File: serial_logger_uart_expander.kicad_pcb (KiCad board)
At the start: 2 copper layers, 95 x 65 mm, 55 parts, among them J1 CN6, J2 CN8, J3 CN5, J4 CN9, J5 Screw_Terminal_01x10, J6 Screw_Terminal_01x10, U1 M74HC4851, U10 2N7002PS, U11 2N7002PS, U12 2N7002PS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

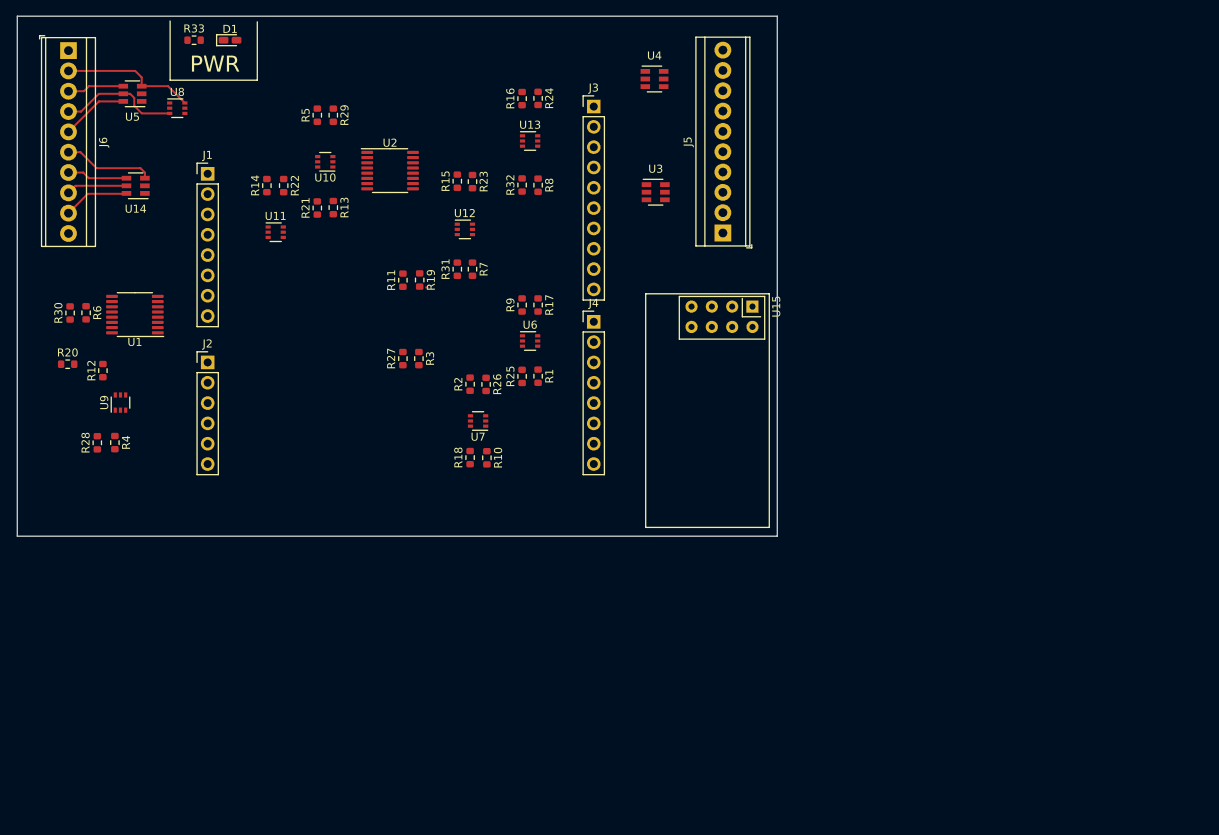
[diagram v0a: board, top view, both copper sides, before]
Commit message: rearranged components and traces
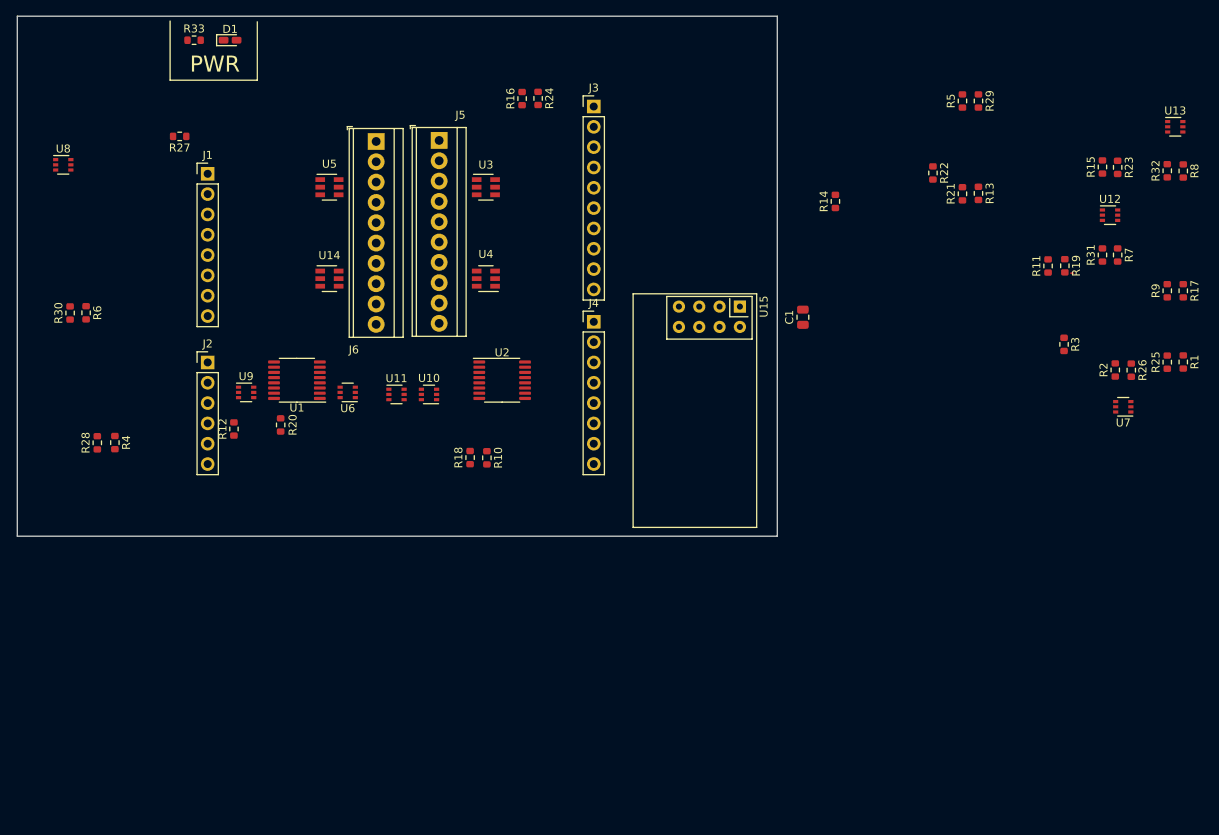
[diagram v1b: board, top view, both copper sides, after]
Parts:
- added C1: 10u, Capacitor_SMD:C_0805_2012Metric, F.Cu at (203.2, 87.6)
- moved R22 81.2 mm to (219.5, 69.6)
- moved R1 80.7 mm to (250.7, 93.2)
- moved R11 80.7 mm to (233.8, 81.2)
- moved R13 80.7 mm to (225.1, 72.1)
- moved R15 80.7 mm to (240.6, 68.8)
- moved R17 80.7 mm to (250.7, 84.3)
- moved R2 80.7 mm to (242.2, 94.2)
- moved R21 80.7 mm to (223.1, 72.2)
- moved R25 80.7 mm to (248.7, 93.2)
- moved R26 80.7 mm to (244.2, 94.2)
- moved R29 80.7 mm to (225.1, 60.6)
- moved R3 80.7 mm to (235.8, 91.0)
- moved R31 80.7 mm to (240.6, 79.8)
- moved R32 80.7 mm to (248.7, 69.3)
- moved R5 80.7 mm to (223.1, 60.6)
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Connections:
- U14 pad 1: Net-(U14-Pad1) -> RX1
- U14 pad 3: TX1 -> Net-(U14-Pad3)
- U14 pad 4: RX1 -> RX0
- U14 pad 6: RX0 -> Net-(U14-Pad6)
- U3 pad 1: Net-(U3-Pad1) -> TX7
- U3 pad 3: TX7 -> TX5
- U3 pad 4: RX7 -> RX6
- U3 pad 6: RX6 -> RX7
- U4 pad 1: Net-(U4-Pad1) -> RX5
- U4 pad 3: TX5 -> Net-(U4-Pad3)
- U4 pad 4: RX5 -> Net-(U4-Pad4)
- U4 pad 5: TX4 -> RX4
- U4 pad 6: RX4 -> TX4
- U5 pad 1: Net-(U5-Pad1) -> TX3
- U5 pad 3: TX3 -> TX1
- U5 pad 4: RX3 -> RX2
- U5 pad 6: RX2 -> RX3
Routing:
- net TX3: track 16.9 -> 0.00 mm
- net TX2: track 15.2 -> 0.00 mm
- net TX1: track 11.3 -> 0.00 mm
- net RX2: track 8.43 -> 0.00 mm
- net RX0: track 8.27 -> 0.00 mm
- net TX0: track 7.61 -> 0.00 mm
- net RX1: track 7.54 -> 0.00 mm
- net RX3: track 7.11 -> 0.00 mm
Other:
- net class JLCPCB added: clearance 0.127, trace_width 0.127, via_dia 0.8, via_drill 0.4
- rule trace_min: 0.2 -> 0.127
- rule via_min_drill: 0.3 -> 0.2

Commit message: completed design, no gerbers or BOM.
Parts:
- moved R23 127.6 mm to (127.0, 123.0)
- moved R8 126.0 mm to (138.3, 126.2), turned to 180 degrees
- moved U13 125.9 mm to (138.2, 122.1)
- moved R32 123.5 mm to (138.3, 124.5), turned to 180 degrees
- moved R11 123.3 mm to (117.2, 121.1), turned to 270 degrees
- moved U12 121.6 mm to (129.6, 122.2), turned to 180 degrees
- moved R15 121.2 mm to (132.2, 123.0)
- moved R3 120.7 mm to (119.9, 124.5), turned to 180 degrees
- moved R19 120.3 mm to (122.5, 121.2), turned to 90 degrees
- moved R7 119.8 mm to (129.6, 119.8), turned to 0 degrees
- moved R31 117.4 mm to (129.6, 118.0), turned to 0 degrees
- moved R17 95.4 mm to (163.6, 123.1)
- moved R29 93.5 mm to (157.0, 124.6), turned to 180 degrees
- moved R5 93.2 mm to (157.1, 126.3), turned to 180 degrees
- moved R9 88.8 mm to (168.9, 123.1)
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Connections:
- U14 pad 1: RX1 -> Net-(U14-Pad1)
- U14 pad 3: Net-(U14-Pad3) -> TX1
- U14 pad 4: RX0 -> RX1
- U14 pad 6: Net-(U14-Pad6) -> RX0
- U3 pad 1: TX7 -> Net-(U3-Pad1)
- U3 pad 3: TX5 -> TX7
- U3 pad 4: RX6 -> RX7
- U3 pad 6: RX7 -> RX6
- U4 pad 1: RX5 -> Net-(U4-Pad1)
- U4 pad 3: Net-(U4-Pad3) -> TX5
- U4 pad 4: Net-(U4-Pad4) -> RX5
- U4 pad 5: RX4 -> TX4
- U4 pad 6: TX4 -> RX4
- U5 pad 1: TX3 -> Net-(U5-Pad1)
- U5 pad 3: TX1 -> TX3
- U5 pad 4: RX2 -> RX3
- U5 pad 6: RX3 -> RX2
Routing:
- net RX_CH1: track 0.00 -> 83.9 mm, vias 0 -> 2
- net RX_CH2: track 0.00 -> 79.2 mm, vias 0 -> 2
- net TX_CH5: track 0.00 -> 57.6 mm, vias 0 -> 2
- net RX_CH3: track 0.00 -> 55.9 mm, vias 0 -> 2
- net TX_CH4: track 0.00 -> 54.2 mm
- net +3V3: track 0.00 -> 52.4 mm
- net RX_CH0: track 0.00 -> 47.9 mm, vias 0 -> 2
- net TX_CH7: track 0.00 -> 45.8 mm, vias 0 -> 2
- net RX_CH6: track 0.00 -> 41.3 mm, vias 0 -> 4
- net TX_CH1: track 0.00 -> 41.2 mm, vias 0 -> 2
- net DATA_TX: track 0.00 -> 41.0 mm, vias 0 -> 1
- net RX_CH4: track 0.00 -> 40.8 mm, vias 0 -> 2
- net TX_CH3: track 0.00 -> 38.8 mm, vias 0 -> 2
- net TX_CH2: track 0.00 -> 38.7 mm, vias 0 -> 2
- net RX_INH: track 0.00 -> 38.6 mm, vias 0 -> 1
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- added copper zone on F.Cu, net +3V3
- added copper zone on B.Cu, net GND
- added copper zone on F.Cu, net VBUS
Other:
- board size 95 x 65 mm -> 95 x 100 mm

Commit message: v0.0 completed
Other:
- outline, holes or cut-outs redrawn
- board text added: "3V3"
- board text added: "5V"
- board text added: "8:1 UART MUX v0.0"
- board text added: "CE"
- board text added: "DATA_RX"
- board text added: "DATA_TX"
- board text added: "GND"
- board text added: "IRQ"
- board text added: "J. Gillispie 2021"
- board text added: "LD2"
- board text added: "MISO"
- board text added: "MOSI"
- board text added: "RX0"
- board text added: "RX1"
- board text added: "RX2"
- board text added: "RX3"
- board text added: "RX4"
- board text added: "RX5"
- board text added: "RX6"
- board text added: "RX7"
- board text added: "RX_A"
- board text added: "RX_B"
- board text added: "RX_C"
- board text added: "RX_INH"
- board text added: "SCK"
- board text added: "TX0"
- board text added: "TX1"
- board text added: "TX2"
- board text added: "TX3"
- board text added: "TX4"
- board text added: "TX5"
- board text added: "TX6"
- board text added: "TX7"
- board text added: "TX_A"
- board text added: "TX_B"
- board text added: "TX_C"
- board text added: "TX_INH"
- board text added: "VBUS"
- board text added: "VCOM_RX"
- board text added: "VCOM_TX"
- board text added: "~CS"
- board text added: "~RST"

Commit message: completed v0.1 design with 2n7002; no BOM or gerbers
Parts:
- removed the J5 at (156.8, 138.9)
- removed the R21 at (159.6, 121.4)
- removed U10, U11, U12, U13, U8, U9: 2N7002PS, my_lib:2N7002PS_NEXPERA_SOT-363
- removed U14: ESDA17-5SC6, my_lib:ESDA17-5SC6_SOT23-6L
- removed the U3 at (162.7, 132.6)
- added J1: Screw_Terminal_01x10, TerminalBlock_TE-Connectivity:TerminalBlock_TE_1-282834-0_1x10_P2.54mm_Horizontal, F.Cu at (126.4, 138.8)
- added Q1: 2N7002, Package_TO_SOT_SMD:SOT-23, F.Cu at (124.1, 124.5)
- added Q10: 2N7002, Package_TO_SOT_SMD:SOT-23, F.Cu at (143.0, 124.5)
- added Q11: 2N7002, Package_TO_SOT_SMD:SOT-23, F.Cu at (155.1, 124.5)
- added Q12: 2N7002, Package_TO_SOT_SMD:SOT-23, F.Cu at (171.2, 124.5)
- added Q13: 2N7002, Package_TO_SOT_SMD:SOT-23, F.Cu at (178.4, 125.7)
- added Q14: 2N7002, Package_TO_SOT_SMD:SOT-23, F.Cu at (135.4, 125.8)
- added Q15: 2N7002, Package_TO_SOT_SMD:SOT-23, F.Cu at (150.6, 125.7)
- added Q16: 2N7002, Package_TO_SOT_SMD:SOT-23, F.Cu at (162.3, 125.7)
- added Q2: 2N7002, Package_TO_SOT_SMD:SOT-23, F.Cu at (139.3, 124.5)
- added Q3: 2N7002, Package_TO_SOT_SMD:SOT-23, F.Cu at (158.7, 124.5)
- added Q4: 2N7002, Package_TO_SOT_SMD:SOT-23, F.Cu at (174.8, 124.5)
- added Q5: 2N7002, Package_TO_SOT_SMD:SOT-23, F.Cu at (131.2, 125.8)
- added Q6: 2N7002, Package_TO_SOT_SMD:SOT-23, F.Cu at (146.6, 125.7)
- added Q7: 2N7002, Package_TO_SOT_SMD:SOT-23, F.Cu at (166.5, 125.7)
- added Q8: 2N7002, Package_TO_SOT_SMD:SOT-23, F.Cu at (182.6, 125.7)
- added Q9: 2N7002, Package_TO_SOT_SMD:SOT-23, F.Cu at (127.7, 124.5)
- added R11: 10k, Resistor_SMD:R_0603_1608Metric, F.Cu at (141.1, 132.0)
- U6, U7: value 2N7002PS -> ESDA17-5SC6; footprint my_lib:2N7002PS_NEXPERA_SOT-363 -> my_lib:ESDA17-5SC6_SOT23-6L
- moved R10 53.6 mm to (134.4, 132.1), turned to 180 degrees
- moved R2 52.3 mm to (132.3, 118.2), turned to 90 degrees
- moved R26 51.2 mm to (134.4, 129.8), turned to 180 degrees
- moved R8 46.0 mm to (183.6, 118.2), turned to 90 degrees
- moved R18 45.9 mm to (136.4, 118.2), turned to 90 degrees
- moved U4 45.3 mm to (130.8, 130.9)
- moved R7 44.3 mm to (173.9, 118.2), turned to 90 degrees
- moved R23 43.5 mm to (170.3, 118.2), turned to 90 degrees
- moved R16 43.2 mm to (177.4, 132.1), turned to 180 degrees
- moved R1 43.2 mm to (123.1, 118.2), turned to 90 degrees
- moved R9 42.6 mm to (127.3, 132.1), turned to 0 degrees
- moved R31 42.1 mm to (170.1, 129.7)
- moved R25 40.3 mm to (127.3, 129.8)
- moved R32 39.5 mm to (177.4, 129.7)
- moved R15 38.9 mm to (170.1, 132.0), turned to 0 degrees
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- renumbered J1 to J2, J2 to J3, J3 to J4, J4 to J5, R11 to R21, U15 to U3
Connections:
- R1 pad 1: TX_CH6 -> RX_CH7
- R10 pad 1: TX_CH5 -> VBUS
- R10 pad 2: +3V3 -> RX6
- R12 pad 1: TX_CH1 -> VBUS
- R12 pad 2: +3V3 -> RX4
- R13 pad 1: RX_CH7 -> VBUS
- R13 pad 2: +3V3 -> RX3
- R14 pad 1: RX_CH5 -> VBUS
- R14 pad 2: +3V3 -> RX2
- R15 pad 1: RX_CH3 -> VBUS
- R15 pad 2: +3V3 -> RX1
- R16 pad 1: RX_CH1 -> VBUS
- R16 pad 2: +3V3 -> RX0
- R17 pad 1: VBUS -> TX_CH7
- R17 pad 2: TX7 -> +3V3
- R18 pad 1: VBUS -> TX_CH6
- R18 pad 2: TX5 -> +3V3
- R19 pad 1: VBUS -> TX_CH5
- R19 pad 2: TX3 -> +3V3
- R2 pad 1: TX_CH4 -> RX_CH6
- R20 pad 1: VBUS -> TX_CH4
- R20 pad 2: TX1 -> +3V3
- R22 pad 1: VBUS -> TX_CH2
- R22 pad 2: RX5 -> +3V3
- R23 pad 1: VBUS -> TX_CH1
- R23 pad 2: RX3 -> +3V3
- R24 pad 1: VBUS -> TX_CH0
- R24 pad 2: RX1 -> +3V3
- R25 pad 2: TX6 -> TX7
- R26 pad 2: TX4 -> TX6
- R27 pad 2: TX2 -> TX5
- R28 pad 2: TX0 -> TX4
- R29 pad 2: RX6 -> TX3
- R3 pad 1: TX_CH2 -> RX_CH5
- R30 pad 2: RX4 -> TX2
- R31 pad 2: RX2 -> TX1
- R32 pad 2: RX0 -> TX0
- R4 pad 1: TX_CH0 -> RX_CH4
- R5 pad 1: RX_CH6 -> RX_CH3
- R6 pad 1: RX_CH4 -> RX_CH2
- R7 pad 1: RX_CH2 -> RX_CH1
- R9 pad 1: TX_CH7 -> VBUS
- R9 pad 2: +3V3 -> RX7
- U1 pad 11: TX_C -> TX_A
- U1 pad 9: TX_A -> TX_C
- U4 pad 3: TX5 -> TX7
- U4 pad 4: RX5 -> RX7
- U4 pad 5: TX4 -> TX6
- U4 pad 6: RX4 -> RX6
- U5 pad 3: TX3 -> TX5
- U5 pad 4: RX3 -> RX5
- U5 pad 5: TX2 -> TX4
- U5 pad 6: RX2 -> RX4
- U6 pad 1: TX_CH7 -> Net-(U6-Pad1)
- U6 pad 2: +3V3 -> GND
- U6 pad 3: TX6 -> TX3
- U6 pad 4: TX_CH6 -> RX3
- U6 pad 5: VBUS -> TX2
- U6 pad 6: TX7 -> RX2
- U7 pad 1: TX_CH5 -> Net-(U7-Pad1)
- U7 pad 2: +3V3 -> GND
- U7 pad 3: TX4 -> TX1
- U7 pad 4: TX_CH4 -> RX1
- U7 pad 5: VBUS -> TX0
- U7 pad 6: TX5 -> RX0
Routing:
- net RX_CH1: track 83.9 -> 38.1 mm
- net RX_CH2: track 79.2 -> 36.0 mm
- net +3V3: track 52.4 -> 14.2 mm, vias 0 -> 2
- net VBUS: track 33.1 -> 0.19 mm
- net RX_CH7: track 31.9 -> 57.8 mm, vias 4 -> 2
- net TX_CH0: track 29.1 -> 53.4 mm, vias 0 -> 2
- net TX_CH5: track 57.6 -> 34.9 mm
- net TX_CH4: track 54.2 -> 32.3 mm
- net TX3: track 36.1 -> 18.9 mm, vias 2 -> 1
- net RX_CH3: track 55.9 -> 39.3 mm
- net TX2: track 31.7 -> 17.3 mm, vias 2 -> 1
- net RX6: track 34.7 -> 20.6 mm
- net TX4: track 31.0 -> 18.6 mm, vias 2 -> 0
- net RX0: track 31.3 -> 19.5 mm, vias 2 -> 0
- net IRQ: track 18.5 -> 29.6 mm
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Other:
- board text added: "8:1 UART MUX v0.1"
- board text removed: "8:1 UART MUX v0.0"

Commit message: ordered from jlcpcb on 09/18/2021, order number W202109180255882; possible to use LCSC components for u4..u7
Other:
- net class JLCPCB: trace_width 0.127 -> 0.2
- rule trace_min: 0.127 -> 0.2
- rule via_min_drill: 0.2 -> 0.3
